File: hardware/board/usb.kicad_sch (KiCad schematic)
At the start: 0 parts

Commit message: emmc stuff
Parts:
- added C118, C119: 100nF X5R 10V, Capacitor_SMD:C_0201_0603Metric, symbol Device:C
- added C120: 1uF X5R 10V, Capacitor_SMD:C_0402_1005Metric, symbol Device:C
- added C121: 100nF X5R 10V, Capacitor_SMD:C_0402_1005Metric, symbol Device:C
- added C122: 120uF SVPF 20V, Capacitor_SMD:CP_Elec_6.3x5.9, symbol Device:C_Polarized
- added D10, D11: BZT52C5V1_C173407, lcsc:SOD-123_L2.7-W1.6-LS3.7-RD, symbol lcsc:BZT52C5V1_C173407
- added J3: USB3_A, symbol Connector:USB3_A
- added L10: L_Iron_Coupled_Small, lcsc:FILTER-SMD_4P-L2.0-W1.2-BL_DLW21H, symbol Device:L_Iron_Coupled_Small
- added R58, R59: 0R 5%, Resistor_SMD:R_0201_0603Metric, symbol Device:R
- added R62, R63: 0R 5%, Resistor_SMD:R_0402_1005Metric, symbol Device:R
- added R64, R65: 2.2R 5%, Resistor_SMD:R_0402_1005Metric, symbol Device:R
- added R66: 4.7K 5%, Resistor_SMD:R_0402_1005Metric, symbol Device:R
- added U14, U15, U16, U17: ESD5311X, lcsc:DFN1006-2L-BI, symbol lcsc:ESD5311X_C2844730
- added U18: SY6280AAC, lcsc:SOT-23-5_L3.0-W1.7-P0.95-LS2.8-BL, symbol lcsc:SY6280AAC
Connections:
- new net: C118.1, J3.9 (SSTX+), U15.2
- new net: L10.3, R63.1, R65.1
- new net: L10.1, R62.2, R64.1
- new net: C119.1, J3.8 (SSTX-), U14.2
- new net: J3.6 (SSRX+), R58.1, U17.2
- new net: J3.5 (SSRX-), R59.1, U16.2
- new net: R66.1, U18.3 (ISET)
- new net GND: C120.1, C121.2, C122.2, D10.2 (A), D11.2 (A), J3.10 (SHIELD), J3.4 (GND), J3.7 (DRAIN), R66.2, U14.1, U15.1, U16.1, U17.1, U18.2 (GND)
- new net USB3_HOST1DM: D11.1 (C), J3.2 (D-), L10.4, R63.2
- new net USB3_HOST1DP: D10.1 (C), J3.3 (D+), L10.2, R62.1
- new net USB3_HOST1_SSRXN: R59.2
- new net USB3_HOST1_SSRXP: R58.2
- new net USB3_HOST1_SSTXN: C119.2
- new net USB3_HOST1_SSTXP: C118.2
- new net USB3_OTG0_DM: R65.2
- new net USB3_OTG0_DP: R64.2
- new net USB_HOST_PWREN_H_GPIO0_A6: U18.4 (EN)
- new net VCC5V0_USB_HOST1: C121.1, C122.1, J3.1 (VBUS), U18.1 (OUT)
- new net VCC_5V0: C120.2, U18.5 (IN)

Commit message: start of ethernet
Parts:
- removed C122: 120uF SVPF 20V, Capacitor_SMD:CP_Elec_6.3x5.9, symbol Device:C_Polarized
- added C122: 47uF X5R 6.3V, Capacitor_SMD:C_0805_2012Metric, symbol Device:C
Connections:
- net GND: now also C122.1
- net VCC5V0_USB_HOST1: now also C122.2
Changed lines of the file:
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@@
+	)
+	(junction
+		(at 82.55 97.79)
+		(diameter 0)
+		(color 0 0 0 0)
+	)
+	(junction
+		(at 82.55 100.33)
+		(diameter 0)
+		(color 0 0 0 0)
+	)
+	(junction
+		(at 78.74 54.61)
+		(diameter 0)
+		(color 0 0 0 0)
+	)
+	(junction
+		(at 60.96 46.99)
+		(diameter 0)
+		(color 0 0 0 0)
+	)
+	(junction
+		(at 72.39 100.33)
+		(diameter 0)
+		(color 0 0 0 0)
 	)
 	(junction
@@
 	)
 	(junction
-		(at 82.55 97.79)
-		(diameter 0)
-		(color 0 0 0 0)
-	)
-	(junction
-		(at 82.55 100.33)
-		(diameter 0)
-		(color 0 0 0 0)
-	)
-	(junction
-		(at 78.74 54.61)
-		(diameter 0)
-		(color 0 0 0 0)
-	)
-	(junction
-		(at 60.96 46.99)
-		(diameter 0)
-		(color 0 0 0 0)
-	)
-	(junction
-		(at 72.39 100.33)
-		(diameter 0)
-		(color 0 0 0 0)
-	)
-	(junction
 		(at 74.93 100.33)
 		(diameter 0)
@@
 	(wire
 		(pts
-			(xy 214.63 107.95) (xy 200.66 107.95)
+			(xy 200.66 107.95) (xy 214.63 107.95)
 		)
 		(stroke
@@
 	(wire
 		(pts
+			(xy 214.63 107.95) (xy 227.33 107.95)
+		)
+		(stroke
+			(width 0)
+			(type default)
+		)
+	)
+	(wire
+		(pts
 			(xy 43.18 62.23) (xy 43.18 63.5)
 		)
@@
 		(pts
 			(xy 201.93 113.03) (xy 201.93 110.49)
-		)
-		(stroke
-			(width 0)
-			(type default)
-		)
-	)
-	(wire
-		(pts
-			(xy 214.63 107.95) (xy 227.33 107.95)
 		)
 		(stroke
@@
 	)
 	(symbol
-		(lib_id "Device:C_Polarized")
-		(at 214.63 111.76 0)
-		(unit 1)
-		(exclude_from_sim no)
-		(in_bom yes)
-		(on_board yes)
-		(dnp no)
-		(property "Reference" "C122"
-			(at 217.678 109.8549 0)
-			(effects
-				(font
-					(size 1.27 1.27)
-				)
-				(justify left)
-			)
-		)
-		(property "Value" "120uF\nSVPF\n20V"
-			(at 217.678 114.3 0)
-			(effects
-				(font
-					(size 1.27 1.27)
-				)
-				(justify left)
-			)
-		)
-		(property "Footprint" "Capacitor_SMD:CP_Elec_6.3x5.9"
-			(at 215.5952 115.57 0)
-			(effects
-				(font
-					(size 1.27 1.27)
-				)
-				(hide yes)
-			)
-		)
-		(property "Datasheet" "~"
-			(at 214.63 111.76 0)
-			(effects
-				(font
-					(size 1.27 1.27)
-				)
-				(hide yes)
-			)
-		)
-		(property "Description" "Polarized capacitor"
-			(at 214.63 111.76 0)
-			(effects
-				(font
-					(size 1.27 1.27)
-				)
-				(hide yes)
-			)
-		)
-		(property "LCSC" "C371973"
-			(at 214.63 111.76 0)
-			(effects
-				(font
-					(size 1.27 1.27)
-				)
-				(hide yes)
-			)
-		)
-		(pin "1"
-		)
-		(pin "2"
-		)
-		(instances
-			(project ""
-				(path "/3bc38516-4fe0-4022-adb8-9fd55b66cd2d/c07c3c7a-b8b0-4fa9-bbf1-2e0263ea0c12"
-					(reference "C122")
-					(unit 1)
-				)
-			)
-		)
-	)
-	(symbol
 		(lib_id "power:GND")
 		(at 66.04 113.03 0)
@@
 					(unit 1)
 				)
+			)
+		)
+	)
+	(symbol
+		(lib_id "Device:C")
+		(at 214.63 111.76 0)
+		(mirror x)
+		(unit 1)
+		(exclude_from_sim no)
+		(in_bom yes)
+		(on_board yes)
+		(dnp no)
+		(property "Reference" "C122"
+			(at 221.488 109.22 0)
+			(effects
+				(font
+					(size 1.27 1.27)
+				)
+				(justify right)
+			)
+		)
+		(property "Value" "47uF\nX5R\n6.3V"
+			(at 221.742 113.538 0)
+			(effects
+				(font
+					(size 1.27 1.27)
+				)
+				(justify right)
+			)
+		)
+		(property "Footprint" "Capacitor_SMD:C_0805_2012Metric"
+			(at 215.5952 107.95 0)
+			(effects
+				(font
+					(size 1.27 1.27)
+				)
+				(hide yes)
+			)
+		)
+		(property "Datasheet" "~"
+			(at 214.63 111.76 0)
+			(effects
+				(font
+					(size 1.27 1.27)
+				)
+				(hide yes)
+			)
+		)
+		(property "Description" "Unpolarized capacitor"
+			(at 214.63 111.76 0)
+			(effects
+				(font
+					(size 1.27 1.27)
+				)
+				(hide yes)
+			)
+		)
+		(pin "2"
+		)
+		(pin "1"
+		)
+		(instances
+			(project "frost"
+				(path "/3bc38516-4fe0-4022-adb8-9fd55b66cd2d/c07c3c7a-b8b0-4fa9-bbf1-2e0263ea0c12"
+					(reference "C122")
+					(unit 1)
+				)

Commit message: finished schematic!
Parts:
- added C339: 100nF X5R 10V, Capacitor_SMD:C_0402_1005Metric, symbol Device:C
- added C340, C342, C344, C345, C346: 100nF X5R 10V, Capacitor_SMD:C_0201_0603Metric, symbol Device:C
- added C341, C343: 4.7uF X5R 6.3V, Capacitor_SMD:C_0402_1005Metric, symbol Device:C
- added U1: RK3568, RK3568:BGA636C65P28X28_1900X1900X168, symbol RK3568:RK3568
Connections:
- net GND: now also C339.2, C340.2, C341.2, C342.2, C343.2, C344.2, C345.2, C346.2
- net USB3_HOST1_SSRXN: now also U1.U28 (USB3_HOST1_SSRXP/SATA1_RXP/QSGMII_RXP_M0)
- net USB3_HOST1_SSRXP: now also U1.U27 (USB3_HOST1_SSRXN/SATA1_RXN/QSGMII_RXN_M0)
- net USB3_HOST1_SSTXN: now also U1.V28 (USB3_HOST1_SSTXP/SATA1_TXP/QSGMII_TXP_M0)
- net USB3_HOST1_SSTXP: now also U1.V27 (USB3_HOST1_SSTXN/SATA1_TXN/QSGMII_TXN_M0)
- net USB3_OTG0_DP: now also U1.P27 (USB3_OTG0_DP), U1.P28 (USB3_OTG0_DM); no longer R64.2
- net USB3_OTG0_DM renamed USB3_HOST1_DM
- net USB3_HOST1_DM: now also U1.P25 (USB3_HOST1_DM)
- new net MULTI_PHY_AVDD_0V9: C340.1, C341.1, U1.R20 (MULTI_PHY_AVDD_0V9), U1.R21 (MULTI_PHY_AVDD_0V9)
- new net PCIE20_REFCLKN: U1.V25 (PCIE20_REFCLKN)
- new net PCIE20_REFCLKP: U1.V24 (PCIE20_REFCLKP)
- new net PCIE20_RXN: U1.Y28 (PCIE20_RXN/SATA2_RXN/QSGMII_RXN_M1)
- new net PCIE20_RXP: U1.Y27 (PCIE20_RXP/SATA2_RXP/QSGMII_RXP_M1)
- new net PCIE20_TXN: U1.W28 (PCIE20_TXN/SATA2_TXN/QSGMII_TXN_M1)
- new net PCIE20_TXP: U1.W27 (PCIE20_TXP/SATA2_TXP/QSGMII_TXP_M1)
- new net USB3_HOST1_DP: R64.2, U1.P24 (USB3_HOST1_DP)
- new net USB3_OTG0_SSRXN: U1.R28 (USB3_OTG0_SSRXP/SATA0_RXP)
- new net USB3_OTG0_SSRXP: U1.R27 (USB3_OTG0_SSRXN/SATA0_RXN)
- new net USB3_OTG0_SSTXN: U1.T28 (USB3_OTG0_SSTXP/SATA0_TXP)
- new net USB3_OTG0_SSTXP: U1.T27 (USB3_OTG0_SSTXN/SATA0_TXN)
- new net USB3_OTG0_VBUSDET: C339.1, U1.M24 (USB3_OTG0_VBUSDET)
- new net USB_AVDD_0V9: C344.1, U1.P22 (USB3_AVDD_0V9)
- new net USB_AVDD_1V8: C345.1, U1.P23 (USB3_AVDD_1V8)
- new net VCCA_1V8: C342.1, C343.1, U1.R22 (MULTI_PHY_AVDD_1V8)
- new net VCC_3V3: C346.1, U1.M23 (USB3_AVDD_3V3)
- no-connect marks 0 -> 12
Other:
- note added: "Diff 100 Ohm ±10%"
- note added: "Diff 85 Ohm ±10%"
- note added: "Diff 90 Ohm ±10%"
- note added: "USB 3.0"
- note added: "for now empty bc no space :("
- moved on the sheet: C120, C121, C122, D10, D11, L10, R62, R63, R64, R65, R66, U18

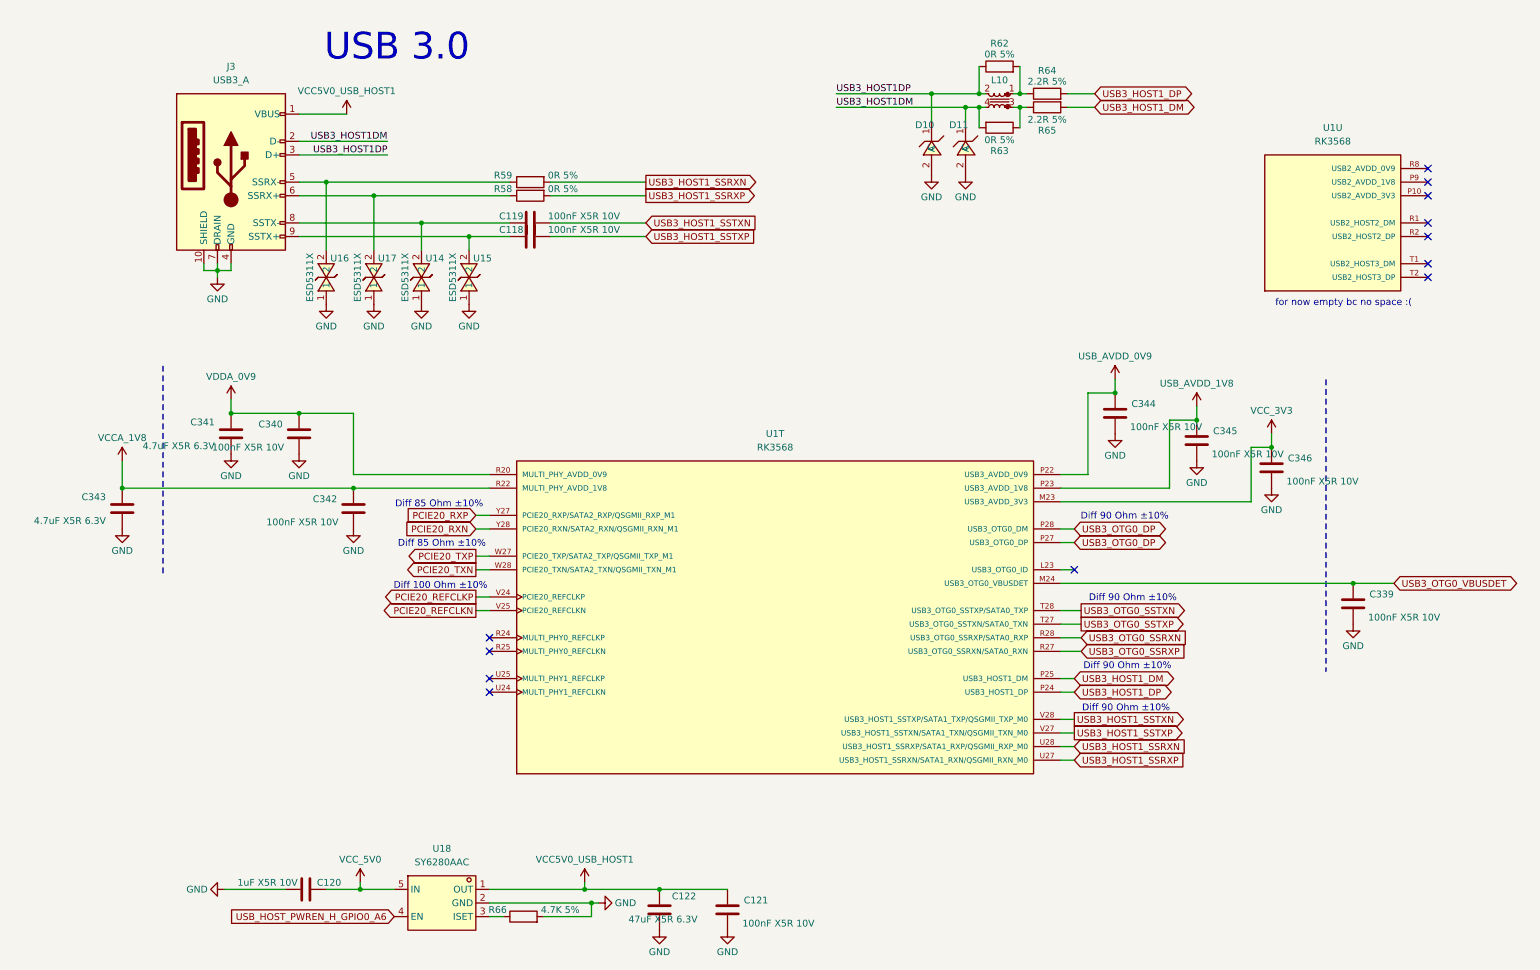
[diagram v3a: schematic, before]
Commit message: finished beautifying schematic
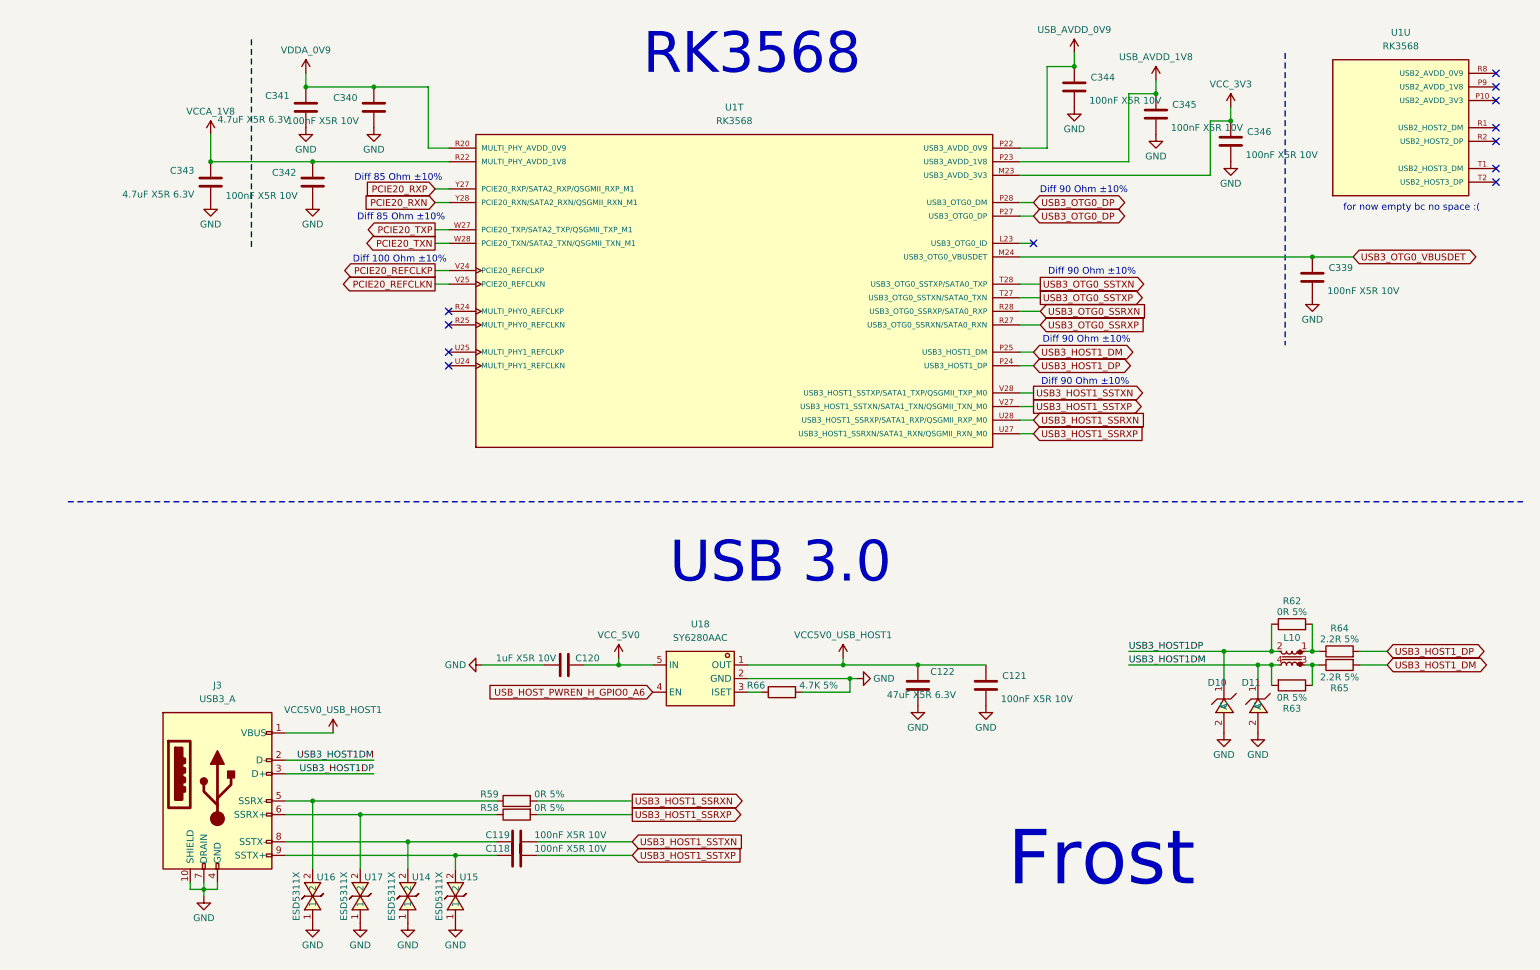
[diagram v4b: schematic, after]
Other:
- note added: "Frost"
- note added: "RK3568"
- moved on the sheet: C118, C119, C120, C121, C122, C339, C340, C341, C342, C343, C344, C345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

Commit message: did a thing
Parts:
- J3: footprint (none) -> lcsc:USB-A-SMD_U-A-39SS-W-1
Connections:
- net USB3_HOST1_SSRXN: now also U1.U27 (USB3_HOST1_SSRXN/SATA1_RXN/QSGMII_RXN_M0); no longer U1.U28 (USB3_HOST1_SSRXP/SATA1_RXP/QSGMII_RXP_M0)
- net USB3_HOST1_SSRXP: now also U1.U28 (USB3_HOST1_SSRXP/SATA1_RXP/QSGMII_RXP_M0); no longer U1.U27 (USB3_HOST1_SSRXN/SATA1_RXN/QSGMII_RXN_M0)
- net USB3_HOST1_SSTXN: now also U1.V27 (USB3_HOST1_SSTXN/SATA1_TXN/QSGMII_TXN_M0); no longer U1.V28 (USB3_HOST1_SSTXP/SATA1_TXP/QSGMII_TXP_M0)
- net USB3_HOST1_SSTXP: now also U1.V28 (USB3_HOST1_SSTXP/SATA1_TXP/QSGMII_TXP_M0); no longer U1.V27 (USB3_HOST1_SSTXN/SATA1_TXN/QSGMII_TXN_M0)
- net USB3_OTG0_DP: no longer U1.P28 (USB3_OTG0_DM)
- net USB3_OTG0_SSRXN: now also U1.R27 (USB3_OTG0_SSRXN/SATA0_RXN); no longer U1.R28 (USB3_OTG0_SSRXP/SATA0_RXP)
- net USB3_OTG0_SSRXP: now also U1.R28 (USB3_OTG0_SSRXP/SATA0_RXP); no longer U1.R27 (USB3_OTG0_SSRXN/SATA0_RXN)
- net USB3_OTG0_SSTXN: now also U1.T27 (USB3_OTG0_SSTXN/SATA0_TXN); no longer U1.T28 (USB3_OTG0_SSTXP/SATA0_TXP)
- net USB3_OTG0_SSTXP: now also U1.T28 (USB3_OTG0_SSTXP/SATA0_TXP); no longer U1.T27 (USB3_OTG0_SSTXN/SATA0_TXN)
- new net USB3_OTG0_DM: U1.P28 (USB3_OTG0_DM)
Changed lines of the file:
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@@
 	(global_label "USB3_HOST1_SSTXP"
 		(shape output)
-		(at 193.04 88.9 0)
+		(at 193.04 86.36 0)
 		(fields_autoplaced yes)
 		(effects
@@
 		)
 		(property "Intersheetrefs" "${INTERSHEET_REFS}"
-			(at 214.8936 88.9 0)
+			(at 214.8936 86.36 0)
 			(effects
 				(font
@@
 	(global_label "USB3_HOST1_SSRXN"
 		(shape input)
-		(at 193.04 91.44 0)
+		(at 193.04 93.98 0)
 		(fields_autoplaced yes)
 		(effects
@@
 		)
 		(property "Intersheetrefs" "${INTERSHEET_REFS}"
-			(at 215.2565 91.44 0)
+			(at 215.2565 93.98 0)
 			(effects
 				(font
@@
 	(global_label "USB3_HOST1_SSRXP"
 		(shape input)
-		(at 193.04 93.98 0)
+		(at 193.04 91.44 0)
 		(fields_autoplaced yes)
 		(effects
@@
 		)
 		(property "Intersheetrefs" "${INTERSHEET_REFS}"
-			(at 215.196 93.98 0)
+			(at 215.196 91.44 0)
 			(effects
 				(font
@@
 	(global_label "USB3_OTG0_SSTXP"
 		(shape output)
-		(at 194.31 68.58 0)
+		(at 194.31 66.04 0)
 		(fields_autoplaced yes)
 		(effects
@@
 		)
 		(property "Intersheetrefs" "${INTERSHEET_REFS}"
-			(at 214.8936 68.58 0)
+			(at 214.8936 66.04 0)
 			(effects
 				(font
@@
 	(global_label "USB3_OTG0_SSRXP"
 		(shape input)
-		(at 194.31 73.66 0)
+		(at 194.31 71.12 0)
 		(fields_autoplaced yes)
 		(effects
@@
 		)
 		(property "Intersheetrefs" "${INTERSHEET_REFS}"
-			(at 215.196 73.66 0)
+			(at 215.196 71.12 0)
 			(effects
 				(font
@@
 		)
 	)
-	(global_label "USB3_OTG0_DP"
+	(global_label "USB3_OTG0_DM"
 		(shape bidirectional)
 		(at 193.04 50.8 0)
@@
 		)
 		(property "Intersheetrefs" "${INTERSHEET_REFS}"
-			(at 211.4088 50.8 0)
+			(at 211.5902 50.8 0)
 			(effects
 				(font
@@
 	(global_label "USB3_OTG0_SSRXN"
 		(shape input)
-		(at 194.31 71.12 0)
+		(at 194.31 73.66 0)
 		(fields_autoplaced yes)
 		(effects
@@
 		)
 		(property "Intersheetrefs" "${INTERSHEET_REFS}"
-			(at 215.2565 71.12 0)
+			(at 215.2565 73.66 0)
 			(effects
 				(font
@@
 	(global_label "USB3_OTG0_SSTXN"
 		(shape output)
-		(at 194.31 66.04 0)
+		(at 194.31 68.58 0)
 		(fields_autoplaced yes)
 		(effects
@@
 		)
 		(property "Intersheetrefs" "${INTERSHEET_REFS}"
-			(at 214.9541 66.04 0)
+			(at 214.9541 68.58 0)
 			(effects
 				(font
@@
 	(global_label "USB3_HOST1_SSTXN"
 		(shape output)
-		(at 193.04 86.36 0)
+		(at 193.04 88.9 0)
 		(fields_autoplaced yes)
 		(effects
@@
 		)
 		(property "Intersheetrefs" "${INTERSHEET_REFS}"
-			(at 214.9541 86.36 0)
+			(at 214.9541 88.9 0)
 			(effects
 				(font
@@
 			)
 		)
-		(property "Footprint" ""
+		(property "Footprint" "lcsc:USB-A-SMD_U-A-39SS-W-1"
 			(at 44.45 157.48 0)
 			(effects
